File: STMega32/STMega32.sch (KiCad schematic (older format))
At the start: 18 parts, among them J1 Conn_01x20, J2 Conn_01x20, Q1 2SC4213, U1 STM32F303R6Tx, U2 LD3985M33R_SOT23

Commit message: Changed microcontroller and rerouted to add ground integrity
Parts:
- removed TP1, TP2, TP3: TestPoint, Measurement_Points:Measurement_Point_Round-SMD-Pad_Small, symbol Connector:TestPoint
- removed U1: STM32F303R6Tx, Package_QFP:LQFP-64_10x10mm_P0.5mm, symbol MCU_ST_STM32F3:STM32F303R6Tx
- added U1: STM32F072RBTx, Package_QFP:LQFP-64_10x10mm_P0.5mm, symbol MCU_ST_STM32F0:STM32F072RBTx
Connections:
- net +3_3v: now also U1.1 (VBAT), U1.13 (VDDA), U1.19 (VDD), U1.32 (VDD), U1.48 (VDDIO2), U1.64 (VDD)
- net CAPS_LED: now also U1.34 (PB13)
- net GND: now also U1.12 (VSSA), U1.18 (VSS), U1.2 (PC13), U1.23 (PA7), U1.24 (PC4), U1.25 (PC5), U1.26 (PB0), U1.27 (PB1), U1.28 (PB2), U1.29 (PB10), U1.3 (PC14), U1.30 (PB11), U1.31 (VSS), U1.33 (PB12), U1.35 (PB14), U1.36 (PB15), U1.4 (PC15), U1.47 (VSS), U1.50 (PA15), U1.55 (PB3), U1.63 (VSS), U1.8 (PC0), U1.9 (PC1)
- net MOSI: now also U1.46 (PA13)
- net SCK: now also U1.49 (PA14)
- net USB_N: now also U1.44 (PA11)
- net USB_P: now also U1.45 (PA12)
- net col0: now also U1.62 (PB9)
- net col1: now also U1.10 (PC2)
- net col10: now also U1.53 (PC12)
- net col11: now also U1.52 (PC11)
- net col12: now also U1.51 (PC10)
- net col13: now also U1.22 (PA6)
- net col14: now also U1.21 (PA5)
- net col15: now also U1.20 (PA4)
- net col16: now also U1.17 (PA3)
- net col17: now also U1.37 (PC6)
- net col2: now also U1.61 (PB8)
- net col3: now also U1.11 (PC3)
- net col4: now also U1.59 (PB7)
- net col5: now also U1.14 (PA0)
- net col6: now also U1.58 (PB6)
- net col7: now also U1.15 (PA1)
- net col8: now also U1.57 (PB5)
- net col9: now also U1.16 (PA2)
- net n_boot: now also U1.60 (BOOT0)
- net row0: now also U1.38 (PC7)
- net row1: now also U1.39 (PC8)
- net row2: now also U1.43 (PA10)
- net row3: now also U1.40 (PC9)
- net row4: now also U1.42 (PA9)
- net row5: now also U1.41 (PA8)
- net NJTRST renamed Reset
- net Reset: now also U1.7 (NRST)
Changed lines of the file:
@@
 Comment4 ""
 $EndDescr
-$Comp
-L MCU_ST_STM32F3:STM32F303R6Tx U1
-U 1 1 6072E398
-P 2350 3050
-F 0 "U1" H 2350 1161 50  0000 C CNN
-F 1 "STM32F303R6Tx" H 2350 1070 50  0000 C CNN
-F 2 "Package_QFP:LQFP-64_10x10mm_P0.5mm" H 1750 1350 50  0001 R CNN
-F 3 "http://www.st.com/st-web-ui/static/active/en/resource/technical/document/datasheet/DM00092070.pdf" H 2350 3050 50  0001 C CNN
-	1    2350 3050
-	1    0    0    -1
-$EndComp
 Text GLabel 3800 2650 2    50   Input ~ 0
 USB_P
@@
 Wire Wire Line
 	3800 2650 3050 2650
-Text GLabel 1000 2750 0    50   Input ~ 0
-OSC_IN_1
-Text GLabel 1000 2650 0    50   Input ~ 0
-OSC_IN_2
-Wire Wire Line
-	1000 2750 1650 2750
-Wire Wire Line
-	1650 2650 1000 2650
 Text GLabel 7450 1800 0    50   Input ~ 0
 col1
@@
 Connection ~ 7550 5050
 Wire Wire Line
-	7550 5050 7650 5050
+	7550 5050 7850 5050
 Wire Wire Line
 	7900 5350 7900 5150
@@
 Connection ~ 8650 5650
 Wire Wire Line
-	8650 5650 8800 5650
+	8650 5650 9000 5650
 Wire Wire Line
 	7900 5550 7900 5650
@@
 Connection ~ 9000 5050
 Wire Wire Line
-	9000 5050 8850 5050
+	9000 5050 8550 5050
 Wire Wire Line
 	8550 5150 8650 5150
@@
 Wire Wire Line
 	3050 4050 3300 4050
-Text GLabel 3650 3550 2    50   Input ~ 0
-NJTRST
-Text GLabel 3650 3450 2    50   Input ~ 0
-SWO
-Text GLabel 3700 2950 2    50   Input ~ 0
-JTDI
 Text GLabel 3700 2850 2    50   Input ~ 0
 SWCLK
@@
 Wire Wire Line
 	3700 2850 3050 2850
-Wire Wire Line
-	3050 2950 3700 2950
-Wire Wire Line
-	3650 3450 3050 3450
-Wire Wire Line
-	3050 3550 3650 3550
 Text GLabel 5550 1400 2    50   Input ~ 0
 MOSI
-Text GLabel 5550 1600 2    50   Input ~ 0
-MISO
 Text GLabel 5550 1500 2    50   Input ~ 0
 SCK
@@
 Text GLabel 5250 1500 0    50   Input ~ 0
 SWCLK
-Text GLabel 5250 1600 0    50   Input ~ 0
-SWO
-Text GLabel 5250 1700 0    50   Input ~ 0
-NJTRST
-Text GLabel 5550 1700 2    50   Input ~ 0
-Reset
 Wire Wire Line
 	5250 1400 5550 1400
 Wire Wire Line
 	5550 1500 5250 1500
-Wire Wire Line
-	5250 1600 5550 1600
-Wire Wire Line
-	5550 1700 5250 1700
 Wire Wire Line
 	1300 4350 1650 4350
@@
 	1500 4550 1500 4450
 $Comp
-L Connector:TestPoint TP2
-U 1 1 607AFF78
-P 8850 5050
-F 0 "TP2" H 8908 5168 50  0000 L CNN
-F 1 "TestPoint" H 8900 5250 50  0000 L CNN
-F 2 "Measurement_Points:Measurement_Point_Round-SMD-Pad_Small" H 9050 5050 50  0001 C CNN
-F 3 "~" H 9050 5050 50  0001 C CNN
-	1    8850 5050
-	1    0    0    -1
-$EndComp
-Connection ~ 8850 5050
-Wire Wire Line
-	8850 5050 8550 5050
-$Comp
-L Connector:TestPoint TP1
-U 1 1 607B0FB7
-P 7650 5050
-F 0 "TP1" H 7450 5200 50  0000 L CNN
-F 1 "TestPoint" H 7500 5300 50  0000 L CNN
-F 2 "Measurement_Points:Measurement_Point_Round-SMD-Pad_Small" H 7850 5050 50  0001 C CNN
-F 3 "~" H 7850 5050 50  0001 C CNN
-	1    7650 5050
-	1    0    0    -1
-$EndComp
-Connection ~ 7650 5050
-Wire Wire Line
-	7650 5050 7850 5050
-$Comp
-L Connector:TestPoint TP3
-U 1 1 607B1547
-P 8800 5650
-F 0 "TP3" H 8750 5700 50  0000 R CNN
-F 1 "TestPoint" H 8750 5800 50  0000 R CNN
-F 2 "Measurement_Points:Measurement_Point_Round-SMD-Pad_Small" H 9000 5650 50  0001 C CNN
-F 3 "~" H 9000 5650 50  0001 C CNN
-	1    8800 5650
-	-1   0    0    1
-$EndComp
-Connection ~ 8800 5650
-Wire Wire Line
-	8800 5650 9000 5650
+L MCU_ST_STM32F0:STM32F072RBTx U1
+U 1 1 608A50E7
+P 2350 3050
+F 0 "U1" H 2350 1161 50  0000 C CNN
+F 1 "STM32F072RBTx" H 2350 1070 50  0000 C CNN
+F 2 "Package_QFP:LQFP-64_10x10mm_P0.5mm" H 1750 1350 50  0001 R CNN
+F 3 "http://www.st.com/st-web-ui/static/active/en/resource/technical/document/datasheet/DM00090510.pdf" H 2350 3050 50  0001 C CNN
+	1    2350 3050
+	1    0    0    -1
+$EndComp
+Wire Wire Line
+	3050 2950 3250 2950
+Wire Wire Line
+	3250 2950 3250 3150
+Wire Wire Line
+	3050 3450 3250 3450
+Wire Wire Line
+	3250 3450 3250 3350
+Connection ~ 3250 3350
 $EndSCHEMATC

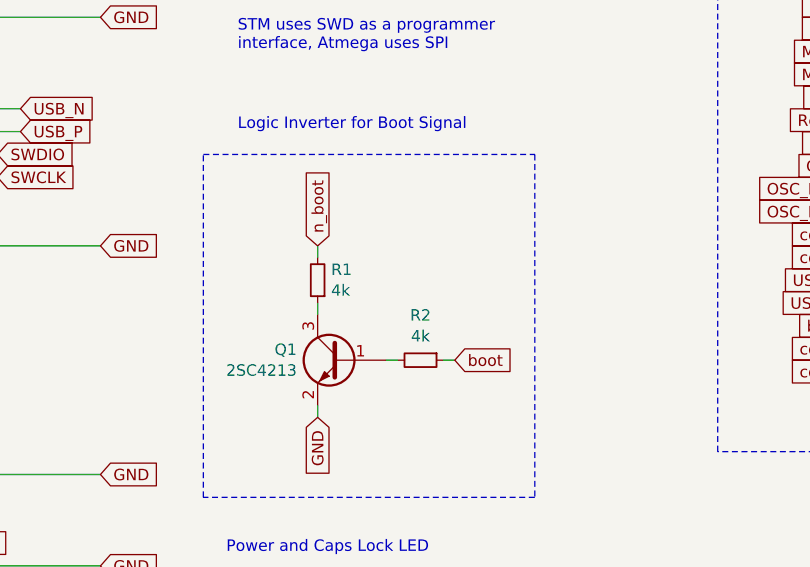
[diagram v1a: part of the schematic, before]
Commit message: removed unused folder, changed R2 on inverter circuit to pullup
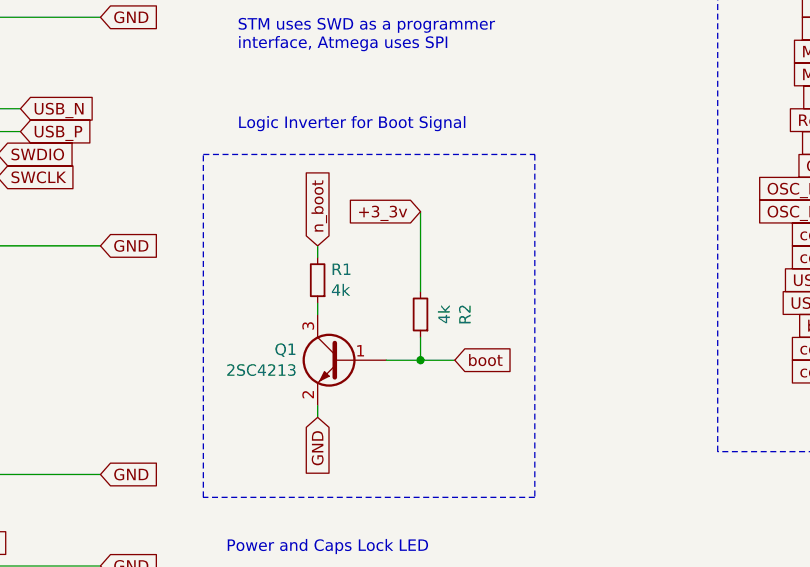
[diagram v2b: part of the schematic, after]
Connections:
- net +3_3v: now also R2.2
- net boot: now also Q1.1 (B)
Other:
- moved on the sheet: R2
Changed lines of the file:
@@
 L Device:R_Small R2
 U 1 1 60743A10
-P 5550 3650
-F 0 "R2" V 5354 3650 50  0000 C CNN
-F 1 "4k" V 5445 3650 50  0000 C CNN
-F 2 "Resistor_SMD:R_0603_1608Metric" H 5550 3650 50  0001 C CNN
-F 3 "~" H 5550 3650 50  0001 C CNN
-	1    5550 3650
-	0    1    1    0
-$EndComp
-Wire Wire Line
-	5400 3650 5450 3650
-Wire Wire Line
-	5650 3650 5700 3650
+P 5550 3450
+F 0 "R2" V 5354 3450 50  0000 C CNN
+F 1 "4k" V 5445 3450 50  0000 C CNN
+F 2 "Resistor_SMD:R_0603_1608Metric" H 5550 3450 50  0001 C CNN
+F 3 "~" H 5550 3450 50  0001 C CNN
+	1    5550 3450
+	-1   0    0    1
+$EndComp
 Text GLabel 5100 3900 3    50   Input ~ 0
 GND
@@
 	3250 3450 3250 3350
 Connection ~ 3250 3350
+Text GLabel 5550 3000 0    50   Input ~ 0
++3_3v
+Wire Wire Line
+	5550 3000 5550 3350
+Wire Wire Line
+	5400 3650 5550 3650
+Wire Wire Line
+	5550 3550 5550 3650
+Connection ~ 5550 3650
+Wire Wire Line
+	5550 3650 5700 3650
 $EndSCHEMATC
